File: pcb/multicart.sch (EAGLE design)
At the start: 16 parts, among them IC1 74HCT373N, IC2 M27C4001B, IC3 74HCT02N, IC4 74HCT00N

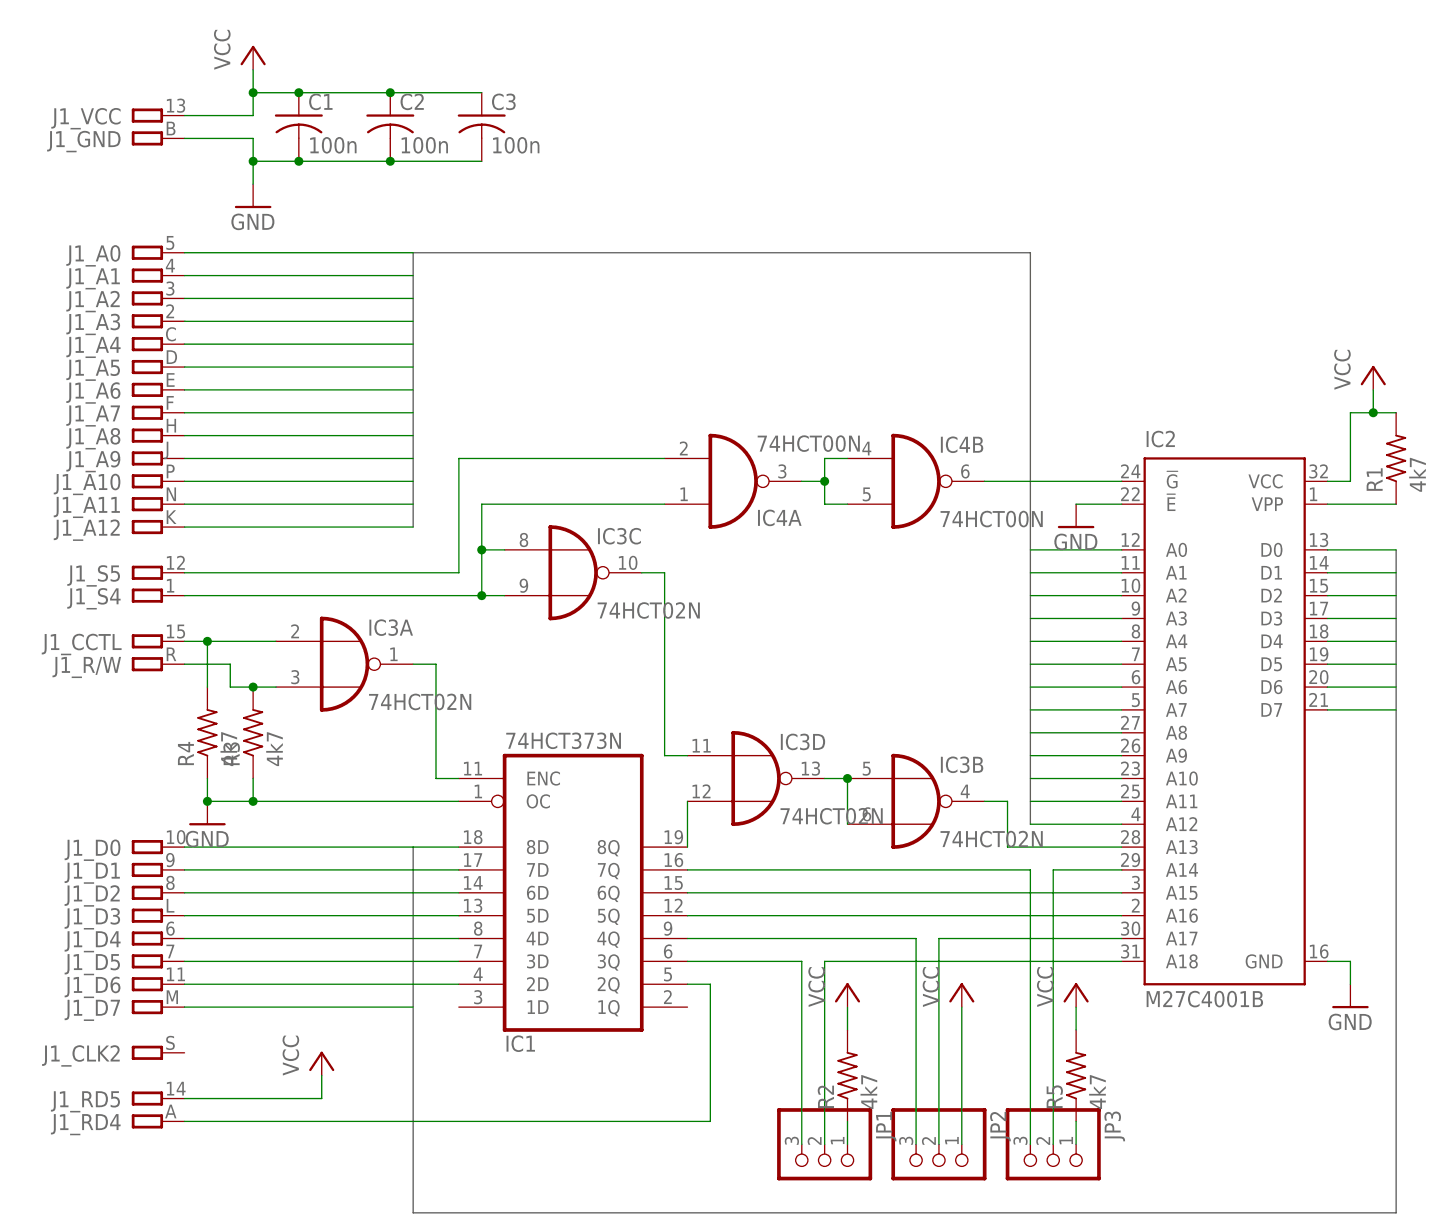
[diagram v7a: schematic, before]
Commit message: Optimized the design by using AND gates.
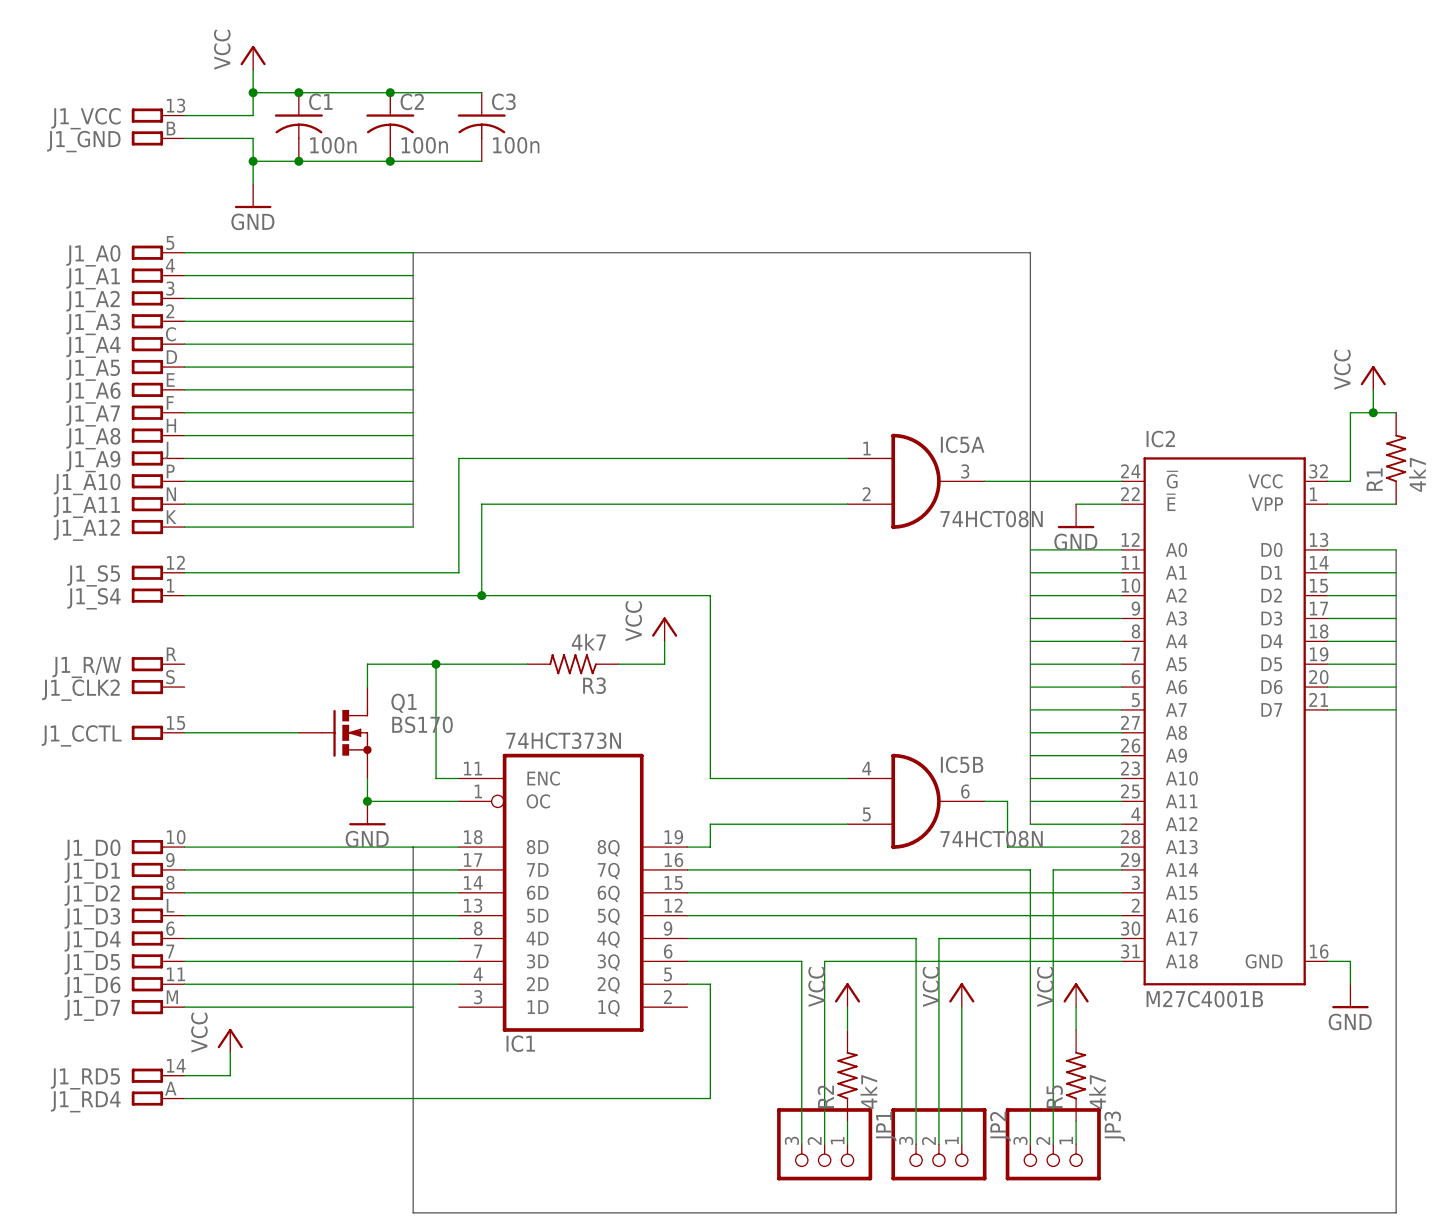
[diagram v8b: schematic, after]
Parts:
- removed IC3: 74HCT02N, 74xx-eu:74HCT02N
- removed IC4: 74HCT00N, 74xx-eu:74HCT00N
- removed R4: 4k7, resistor:R-US_0204/7
- added IC5: 74HCT08N, 74xx-eu:74HCT08N
- added Q1: BS170, transistor-small-signal:BS170
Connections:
- removed net N$14: IC4A.O, IC4B.I0, IC4B.I1
- removed net N$17: IC3C.O, IC3D.I0
- removed net N$20: IC3A.I1, J1_R/W.P, R3.2
- removed net N$23: IC3B.I0, IC3B.I1, IC3D.O
- net GND: now also Q1.S; no longer R3.1, R4.1
- net N$1: now also IC5B.I1; no longer IC3D.I1
- net N$18: now also IC5A.I0; no longer IC4A.I1
- net N$19: now also IC5A.I1, IC5B.I0; no longer IC3C.I0, IC3C.I1, IC4A.I0
- net N$21: now also IC5B.O; no longer IC3B.O
- net N$27: now also IC5A.O; no longer IC4B.O
- net N$7: now also Q1.D, R3.2; no longer IC3A.O
- net N$8: now also Q1.G; no longer IC3A.I0, R4.2
- net VCC: now also R3.1
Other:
- moved on the sheet: J1_CCTL, J1_CLK2, J1_RD4, J1_RD5, R3
